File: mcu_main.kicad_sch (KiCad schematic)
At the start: 10 parts

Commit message: all submodules added
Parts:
- added D? (x2): D_TVS, Diode_SMD:D_1206_3216Metric_Pad1.42x1.75mm_HandSolder, symbol Device:D_TVS
- added J?: USB_C_Receptacle_USB2.0, symbol Connector:USB_C_Receptacle_USB2.0
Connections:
- net +5V: now also J?.A4 (VBUS), J?.A9 (VBUS), J?.B4 (VBUS), J?.B9 (VBUS)
- net D+: now also D?.2 (A2)
- net D-: now also D?.2 (A2)
- net GND: now also J?.A1 (GND), J?.A12 (GND), J?.B1 (GND), J?.B12 (GND), J?.S1 (SHIELD)
- new net: D?.1 (A1), J?.A6 (D+), J?.B6 (D+)
- new net: D?.1 (A1), J?.A7 (D-), J?.B7 (D-)
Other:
- note added: "USB"
- moved on the sheet: C?, R?, SW?, U?, Y?

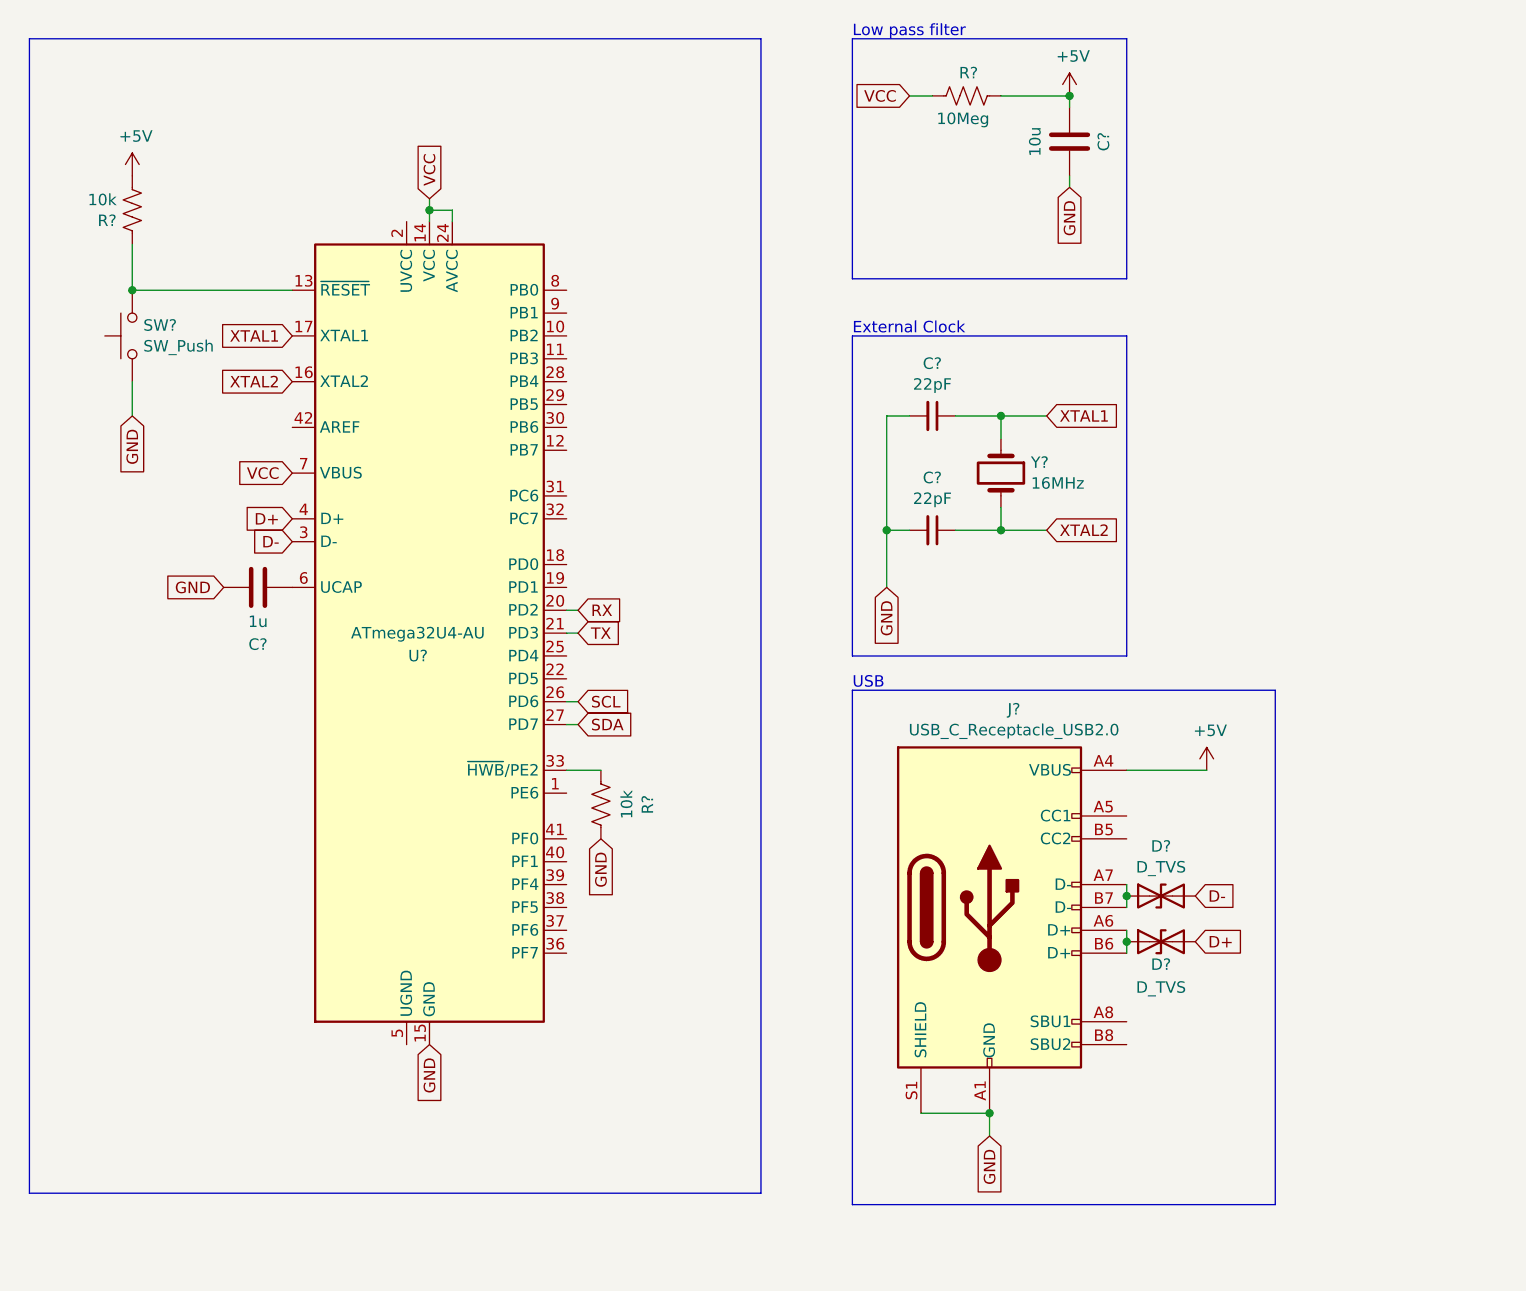
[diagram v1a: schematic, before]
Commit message: added hierarchical labels
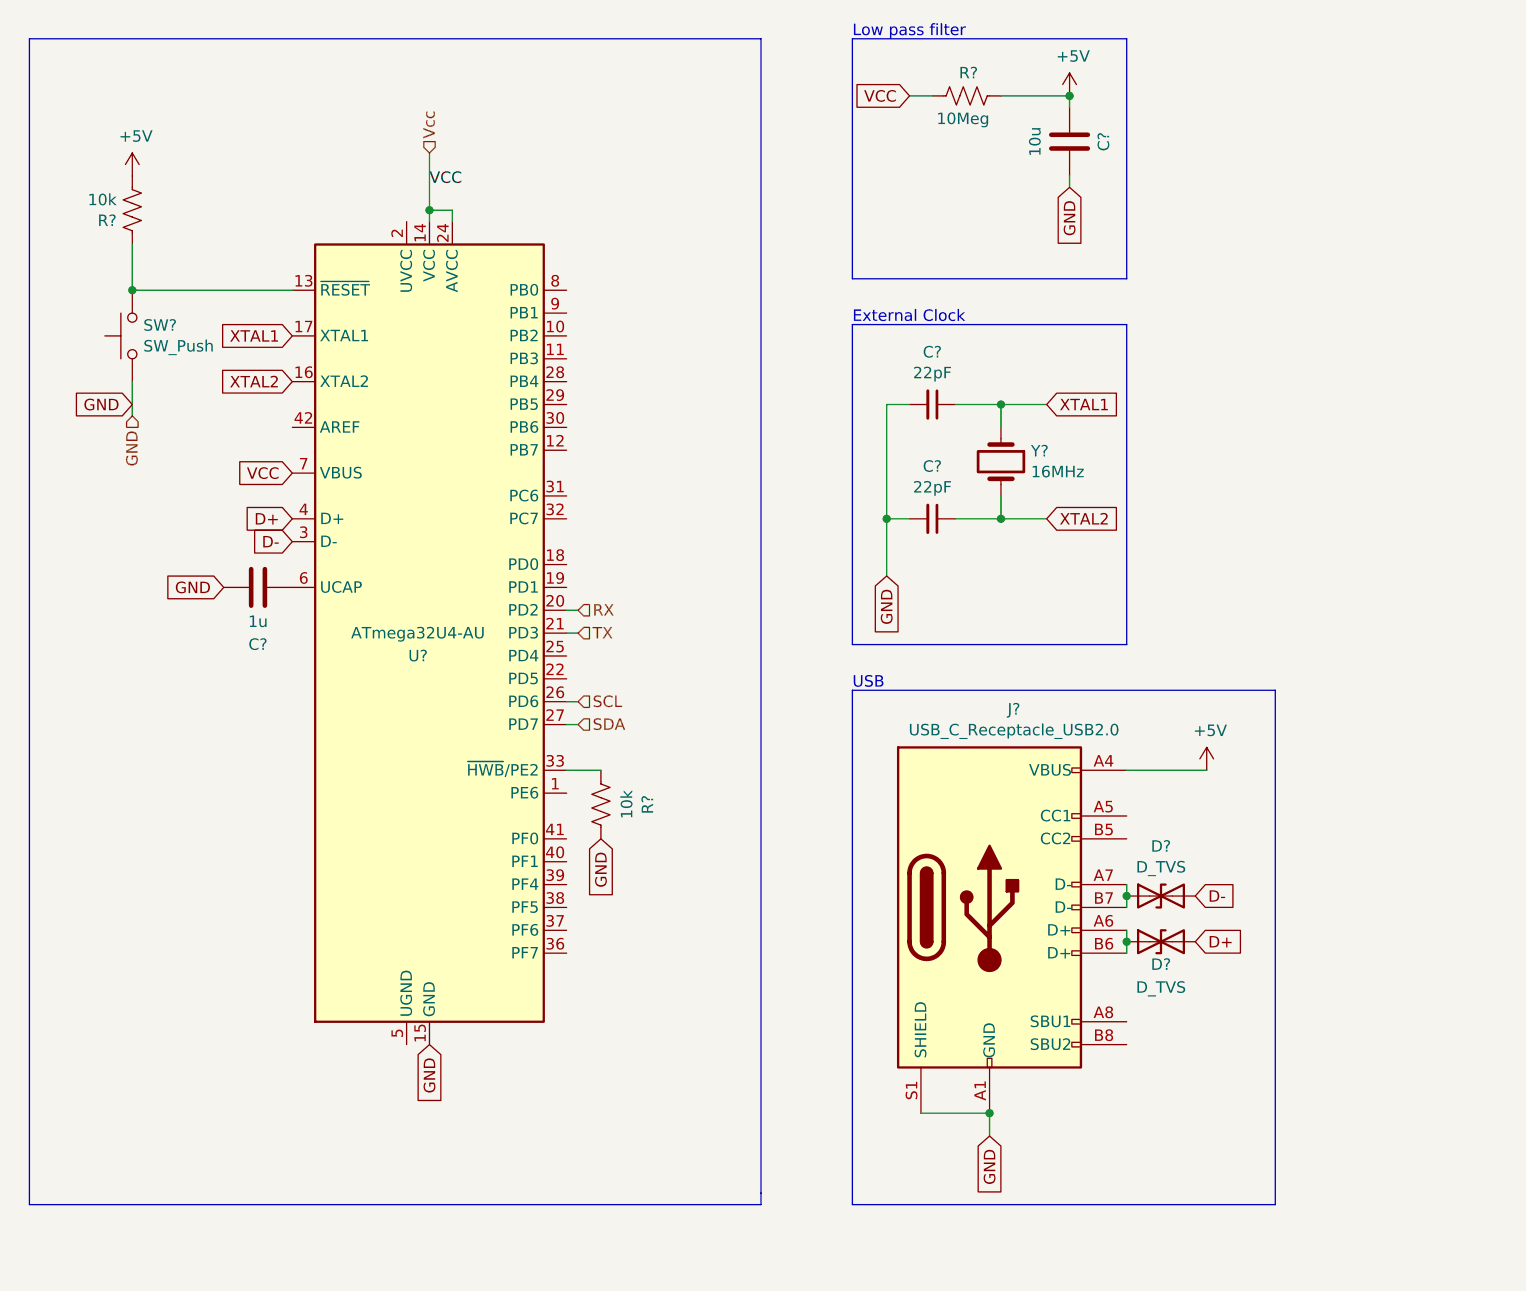
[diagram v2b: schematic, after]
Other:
- moved on the sheet: C?, Y?

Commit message: updated UPD module
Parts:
- removed D? (x2): D_TVS, Diode_SMD:D_1206_3216Metric_Pad1.42x1.75mm_HandSolder, symbol Device:D_TVS
- removed J?: USB_C_Receptacle_USB2.0, symbol Connector:USB_C_Receptacle_USB2.0
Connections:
- net MOSI: now reaches U?.10 (PB2)
- net MISO: now reaches U?.11 (PB3)
- net ~{SS}: now reaches U?.8 (PB0)
- net SCK: now reaches U?.9 (PB1)
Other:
- note removed: "USB"
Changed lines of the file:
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@@
   (junction (at 111.76 40.64) (diameter 0) (color 0 0 0 0))
   (junction (at 162.56 74.93) (diameter 0) (color 0 0 0 0))
-  (junction (at 173.99 140.97) (diameter 0) (color 0 0 0 0))
   (junction (at 175.26 62.23) (diameter 0) (color 0 0 0 0))
   (junction (at 175.26 74.93) (diameter 0) (color 0 0 0 0))
   (junction (at 182.88 27.94) (diameter 0) (color 0 0 0 0))
-  (junction (at 189.23 116.84) (diameter 0) (color 0 0 0 0))
-  (junction (at 189.23 121.92) (diameter 0) (color 0 0 0 0))
   (wire (pts (xy 78.74 44.45) (xy 78.74 49.53))
     (stroke (width 0) (type default) (color 0 0 0 0))
@@
     (stroke (width 0) (type default) (color 0 0 0 0))
   )
+  (wire (pts (xy 127 49.53) (xy 128.27 49.53))
+    (stroke (width 0) (type default) (color 0 0 0 0))
+  )
+  (wire (pts (xy 127 52.07) (xy 128.27 52.07))
+    (stroke (width 0) (type default) (color 0 0 0 0))
+  )
+  (wire (pts (xy 127 54.61) (xy 128.27 54.61))
+    (stroke (width 0) (type default) (color 0 0 0 0))
+  )
+  (wire (pts (xy 127 57.15) (xy 128.27 57.15))
+    (stroke (width 0) (type default) (color 0 0 0 0))
+  )
   (wire (pts (xy 127 85.09) (xy 128.27 85.09))
     (stroke (width 0) (type default) (color 0 0 0 0))
@@
     (stroke (width 0) (type default) (color 0 0 0 0))
   )
-  (wire (pts (xy 166.37 140.97) (xy 173.99 140.97))
-    (stroke (width 0) (type default) (color 0 0 0 0))
-  )
   (wire (pts (xy 170.18 62.23) (xy 175.26 62.23))
     (stroke (width 0) (type default) (color 0 0 0 0))
   )
-  (wire (pts (xy 173.99 140.97) (xy 173.99 143.51))
-    (stroke (width 0) (type default) (color 0 0 0 0))
-  )
   (wire (pts (xy 175.26 27.94) (xy 182.88 27.94))
     (stroke (width 0) (type default) (color 0 0 0 0))
@@
     (stroke (width 0) (type default) (color 0 0 0 0))
   )
-  (wire (pts (xy 189.23 102.87) (xy 198.12 102.87))
-    (stroke (width 0) (type default) (color 0 0 0 0))
-  )
-  (wire (pts (xy 189.23 116.84) (xy 189.23 115.57))
-    (stroke (width 0) (type default) (color 0 0 0 0))
-  )
-  (wire (pts (xy 189.23 118.11) (xy 189.23 116.84))
-    (stroke (width 0) (type default) (color 0 0 0 0))
-  )
-  (wire (pts (xy 189.23 121.92) (xy 189.23 120.65))
-    (stroke (width 0) (type default) (color 0 0 0 0))
-  )
-  (wire (pts (xy 189.23 123.19) (xy 189.23 121.92))
-    (stroke (width 0) (type default) (color 0 0 0 0))
-  )
   (polyline (pts (xy 67.31 21.59) (xy 67.31 149.86))
     (stroke (width 0) (type default) (color 0 0 0 0))
@@
     (stroke (width 0) (type default) (color 0 0 0 0))
   )
-  (polyline (pts (xy 158.75 93.98) (xy 158.75 151.13))
-    (stroke (width 0) (type default) (color 0 0 0 0))
-  )
-  (polyline (pts (xy 158.75 151.13) (xy 205.74 151.13))
-    (stroke (width 0) (type default) (color 0 0 0 0))
-  )
   (polyline (pts (xy 189.23 21.59) (xy 189.23 48.26))
     (stroke (width 0) (type default) (color 0 0 0 0))
@@
   )
   (polyline (pts (xy 189.23 88.9) (xy 158.75 88.9))
-    (stroke (width 0) (type default) (color 0 0 0 0))
-  )
-  (polyline (pts (xy 205.74 93.98) (xy 158.75 93.98))
-    (stroke (width 0) (type default) (color 0 0 0 0))
-  )
-  (polyline (pts (xy 205.74 93.98) (xy 205.74 151.13))
     (stroke (width 0) (type default) (color 0 0 0 0))
   )
@@
     (effects (font (size 1.27 1.27)) (justify left bottom))
   )
-  (text "USB" (at 158.75 93.98 0)
-    (effects (font (size 1.27 1.27)) (justify left bottom))
-  )
   (label "VCC" (at 111.76 38.1 0)
     (effects (font (size 1.27 1.27)) (justify left bottom))
@@
     )
   )
-  (global_label "GND" (shape input) (at 173.99 143.51 270) (fields_autoplaced)
-    (effects (font (size 1.27 1.27)) (justify right))
-    (property "Intersheet References" "${INTERSHEET_REFS}" (id 0) (at 46.99 11.43 0)
-      (effects (font (size 1.27 1.27)) hide)
-    )
-  )
   (global_label "XTAL1" (shape input) (at 180.34 62.23 0) (fields_autoplaced)
     (effects (font (size 1.27 1.27)) (justify left))
@@
     )
   )
-  (global_label "D-" (shape input) (at 196.85 116.84 0) (fields_autoplaced)
-    (effects (font (size 1.27 1.27)) (justify left))
-    (property "Intersheet References" "${INTERSHEET_REFS}" (id 0) (at 46.99 11.43 0)
-      (effects (font (size 1.27 1.27)) hide)
-    )
-  )
-  (global_label "D+" (shape input) (at 196.85 121.92 0) (fields_autoplaced)
-    (effects (font (size 1.27 1.27)) (justify left))
-    (property "Intersheet References" "${INTERSHEET_REFS}" (id 0) (at 46.99 11.43 0)
-      (effects (font (size 1.27 1.27)) hide)
-    )
-  )
   (hierarchical_label "GND" (shape input) (at 78.74 63.5 270)
     (effects (font (size 1.27 1.27)) (justify right))
   )
   (hierarchical_label "Vcc" (shape input) (at 111.76 34.29 90)
+    (effects (font (size 1.27 1.27)) (justify left))
+  )
+  (hierarchical_label "~{SS}" (shape input) (at 128.27 49.53 0)
+    (effects (font (size 1.27 1.27)) (justify left))
+  )
+  (hierarchical_label "SCK" (shape input) (at 128.27 52.07 0)
+    (effects (font (size 1.27 1.27)) (justify left))
+  )
+  (hierarchical_label "MOSI" (shape input) (at 128.27 54.61 0)
+    (effects (font (size 1.27 1.27)) (justify left))
+  )
+  (hierarchical_label "MISO" (shape input) (at 128.27 57.15 0)
     (effects (font (size 1.27 1.27)) (justify left))
   )
@@
     )
     (property "Datasheet" "" (id 3) (at 182.88 27.94 0)
-      (effects (font (size 1.27 1.27)) hide)
-    )
-    (pin "1")
-  )
-  (symbol (lib_id "power:+5V") (at 198.12 102.87 0) (unit 1)
-    (in_bom yes) (on_board yes)
-    (property "Reference" "#PWR?" (id 0) (at 198.12 106.68 0)
-      (effects (font (size 1.27 1.27)) hide)
-    )
-    (property "Value" "+5V" (id 1) (at 198.501 98.4758 0))
-    (property "Footprint" "" (id 2) (at 198.12 102.87 0)
-      (effects (font (size 1.27 1.27)) hide)
-    )
-    (property "Datasheet" "" (id 3) (at 198.12 102.87 0)
       (effects (font (size 1.27 1.27)) hide)
     )
@@
     (pin "2")
   )
-  (symbol (lib_id "Device:D_TVS") (at 193.04 116.84 0) (unit 1)
-    (in_bom yes) (on_board yes)
-    (property "Reference" "D?" (id 0) (at 193.04 111.3282 0))
-    (property "Value" "D_TVS" (id 1) (at 193.04 113.6396 0))
-    (property "Footprint" "Diode_SMD:D_1206_3216Metric_Pad1.42x1.75mm_HandSolder" (id 2) (at 193.04 116.84 0)
-      (effects (font (size 1.27 1.27)) hide)
-    )
-    (property "Datasheet" "~" (id 3) (at 193.04 116.84 0)
-      (effects (font (size 1.27 1.27)) hide)
-    )
-    (pin "1")
-    (pin "2")
-  )
-  (symbol (lib_id "Device:D_TVS") (at 193.04 121.92 0) (unit 1)
-    (in_bom yes) (on_board yes)
-    (property "Reference" "D?" (id 0) (at 193.04 124.46 0))
-    (property "Value" "D_TVS" (id 1) (at 193.04 127 0))
-    (property "Footprint" "Diode_SMD:D_1206_3216Metric_Pad1.42x1.75mm_HandSolder" (id 2) (at 193.04 121.92 0)
-      (effects (font (size 1.27 1.27)) hide)
-    )
-    (property "Datasheet" "~" (id 3) (at 193.04 121.92 0)
-      (effects (font (size 1.27 1.27)) hide)
-    )
-    (pin "1")
-    (pin "2")
-  )
   (symbol (lib_id "Device:C") (at 92.71 82.55 270) (unit 1)
     (in_bom yes) (on_board yes)
@@
     (pin "2")
   )
-  (symbol (lib_id "Connector:USB_C_Receptacle_USB2.0") (at 173.99 118.11 0) (unit 1)
-    (in_bom yes) (on_board yes)
-    (property "Reference" "J?" (id 0) (at 176.7078 96.0882 0))
-    (property "Value" "USB_C_Receptacle_USB2.0" (id 1) (at 176.7078 98.3996 0))
-    (property "Footprint" "" (id 2) (at 177.8 118.11 0)
-      (effects (font (size 1.27 1.27)) hide)
-    )
-    (property "Datasheet" "https://www.usb.org/sites/default/files/documents/usb_type-c.zip" (id 3) (at 177.8 118.11 0)
-      (effects (font (size 1.27 1.27)) hide)
-    )
-    (pin "A1")
-    (pin "A12")
-    (pin "A4")
-    (pin "A5")
-    (pin "A6")
-    (pin "A7")
-    (pin "A8")
-    (pin "A9")
-    (pin "B1")
-    (pin "B12")
-    (pin "B4")
-    (pin "B5")
-    (pin "B6")
-    (pin "B7")
-    (pin "B8")
-    (pin "B9")
-    (pin "S1")
-  )
   (symbol (lib_id "MCU_Microchip_ATmega:ATmega32U4-AU") (at 111.76 87.63 0) (unit 1)

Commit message: update after meeting on tues
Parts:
- removed C? (x2): 22pF, Capacitor_SMD:C_0603_1608Metric_Pad1.08x0.95mm_HandSolder, symbol Device:C_Small
- removed Y?: 16MHz, symbol Device:Crystal
- added Y?: 16M, Crystal:Resonator_SMD_muRata_CDSCB-2Pin_4.5x2.0mm_HandSoldering, symbol Device:Resonator
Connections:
- net +5V: now also R?.1; no longer C?.2, R?.2
- net VCC: no longer R?.1
- net at R?.1, SW?.2: no longer U?.13 (~{RESET})
- net XTAL1: no longer names the net of U?.17 (XTAL1)
- net XTAL1: now also Y?.1
- net XTAL2: no longer names the net of U?.16 (XTAL2)
- net XTAL2: now also Y?.3
- new net AREF: C?.2, R?.2
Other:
- note removed: "External Clock"
- moved on the sheet: R?, SW?

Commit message: added TODOs and comments
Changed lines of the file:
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@@
     (effects (font (size 1.27 1.27)) (justify left bottom))
   )
-  (label "ICSP in-circuit serial programming" (at 157.48 62.23 0)
+  (label "ICSP in-circuit serial programming for debug" (at 157.48 62.23 0)
     (effects (font (size 1.27 1.27)) (justify left bottom))
   )

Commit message: updated schematic
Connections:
- net at U?.13 (~{RESET}): now also R?.1, SW?.2
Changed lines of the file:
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@@
 (kicad_sch (version 20210621) (generator eeschema)
   (paper "A4")
+  (junction (at 73.66 49.53) (diameter 0) (color 0 0 0 0))
   (junction (at 111.76 40.64) (diameter 0) (color 0 0 0 0))
   (junction (at 181.61 27.94) (diameter 0) (color 0 0 0 0))
   (junction (at 182.88 29.21) (diameter 0) (color 0 0 0 0))
   (wire (pts (xy 73.66 44.45) (xy 73.66 49.53))
+    (stroke (width 0) (type default) (color 0 0 0 0))
+  )
+  (wire (pts (xy 73.66 49.53) (xy 96.52 49.53))
     (stroke (width 0) (type default) (color 0 0 0 0))
   )
@@
   )
   (wire (pts (xy 93.98 60.96) (xy 90.17 60.96))
-    (stroke (width 0) (type default) (color 0 0 0 0))
-  )
-  (wire (pts (xy 96.52 49.53) (xy 78.74 49.53))
     (stroke (width 0) (type default) (color 0 0 0 0))
   )
@@
     )
   )
-  (global_label "INTerrupt" (shape input) (at 160.02 102.87 0) (fields_autoplaced)
+  (global_label "INTerrupt" (shape input) (at 156.21 78.74 0) (fields_autoplaced)
     (effects (font (size 1.27 1.27)) (justify left))
-    (property "Intersheet References" "${INTERSHEET_REFS}" (id 0) (at 170.9318 102.7906 0)
+    (property "Intersheet References" "${INTERSHEET_REFS}" (id 0) (at 167.1218 78.6606 0)
       (effects (font (size 1.27 1.27)) (justify left) hide)
     )

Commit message: updated for winter 2022
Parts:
- added J?: Conn_02x03_Odd_Even, symbol Connector_Generic:Conn_02x03_Odd_Even
- gave numbers to parts that had none: 8
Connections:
- net GND: no longer C1.2, C2.1, R2.1, U1.15 (GND), U1.23 (GND), U1.35 (GND), U1.43 (GND)
- net MISO: now also J?.1 (Pin_1)
- net MOSI: now also J?.4 (Pin_4)
- net SCK: now also J?.3 (Pin_3)
- net ~{RESET}: now reaches R1.1, SW1.2, U1.13 (~{RESET})
- net ~{RESET}: now also J?.5 (Pin_5)
- net PCINT4: now reaches U1.28 (PB4)
- net PCINT5: now reaches U1.29 (PB5)
- net PCINT6: now reaches U1.30 (PB6)
- net RX renamed IN2/RX
- net SCL: no longer names the net of U1.26 (PD6)
- net SDA: no longer names the net of U1.27 (PD7)
- net TX renamed INT3/TX
- net VCC renamed Vcc
- net Vcc: now also J?.2 (Pin_2)
- net ~{SS} renamed PCINT0
- new net Earth: C1.2, C2.1, J?.6 (Pin_6), R2.1, U1.15 (GND), U1.23 (GND), U1.35 (GND), U1.43 (GND)
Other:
- note added: "ICSP Connector"
